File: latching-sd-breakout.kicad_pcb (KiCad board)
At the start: 2 copper layers, 25.5 x 23.8 mm, 7 parts, among them X1 microSD

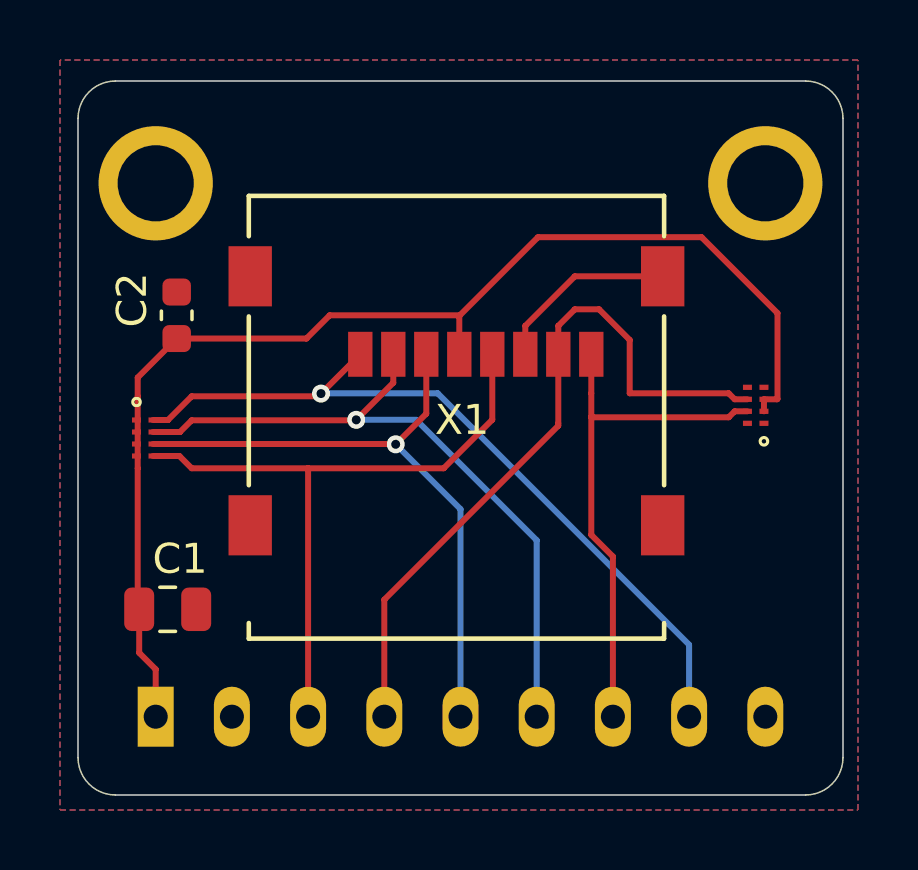
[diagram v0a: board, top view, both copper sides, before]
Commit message: replace 0502 resister arrays with 0603
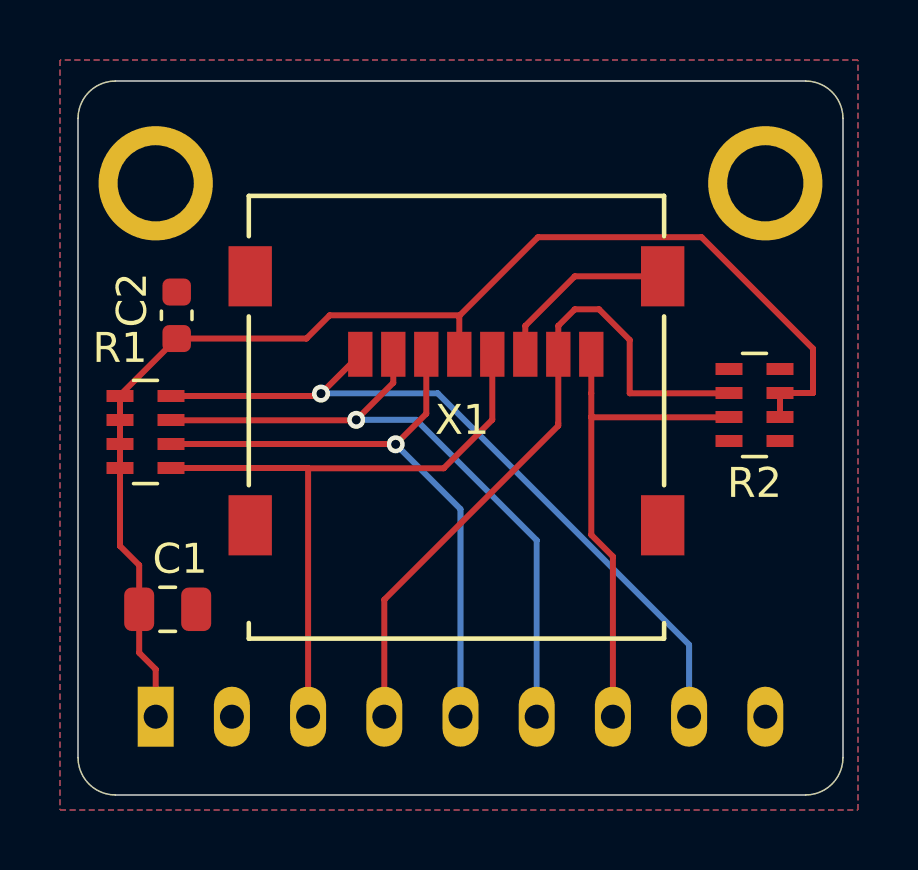
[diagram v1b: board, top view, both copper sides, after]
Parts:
- R1, R2: footprint Resistor_SMD:R_Array_Convex_4x0502 -> Resistor_SMD:R_Array_Concave_4x0603
- moved R1 0.20 mm to (114.5, 96.8), turned to 0 degrees
- turned R2 to 180 degrees
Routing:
- net 3.3V: track 40.9 -> 43.0 mm
- net /DAT2: track 26.0 -> 25.0 mm
- net /SCLK: track 22.6 -> 21.8 mm
- net /CS: track 23.2 -> 22.4 mm
- net /DAT1: track 17.7 -> 17.0 mm
- net /DO: track 24.2 -> 23.5 mm
- net /DI: track 21.5 -> 20.9 mm
